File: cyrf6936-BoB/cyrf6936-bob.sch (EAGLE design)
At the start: 23 parts

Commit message: Added revision and author
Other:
- note added: "Joseph Moreland"
- note added: "v0.1"
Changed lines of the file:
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@@
 Load Capacitance 10pF
 </text>
+<text x="182.88" y="7.62" size="2.1844" layer="97">Joseph Moreland</text>
+<text x="236.22" y="7.62" size="2.1844" layer="97">v0.1</text>
 </plain>
 <instances>

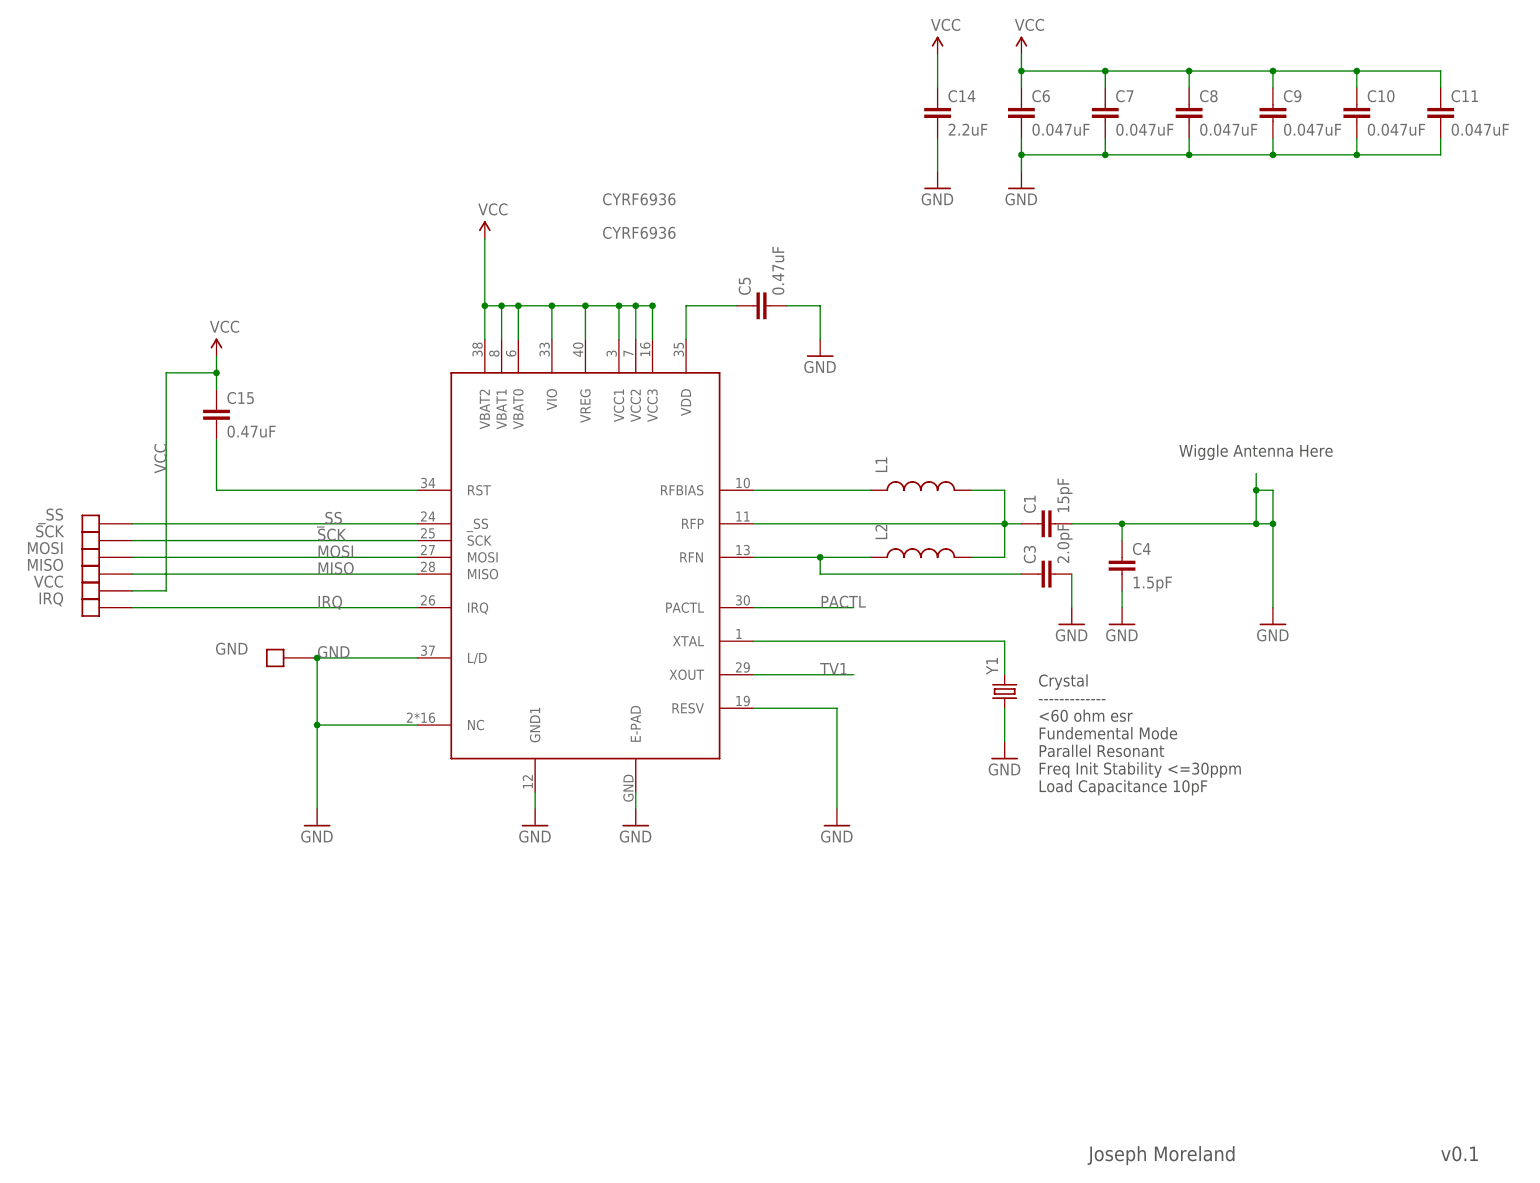
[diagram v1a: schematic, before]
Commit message: Screwed up that last commit.  this update include changes to the production gerber folders.  Adds hackvana to the cyrf6936-BoB and cleans up the fab notes a bit.  Still need to standardize and parameterize the creation of the gerbers.
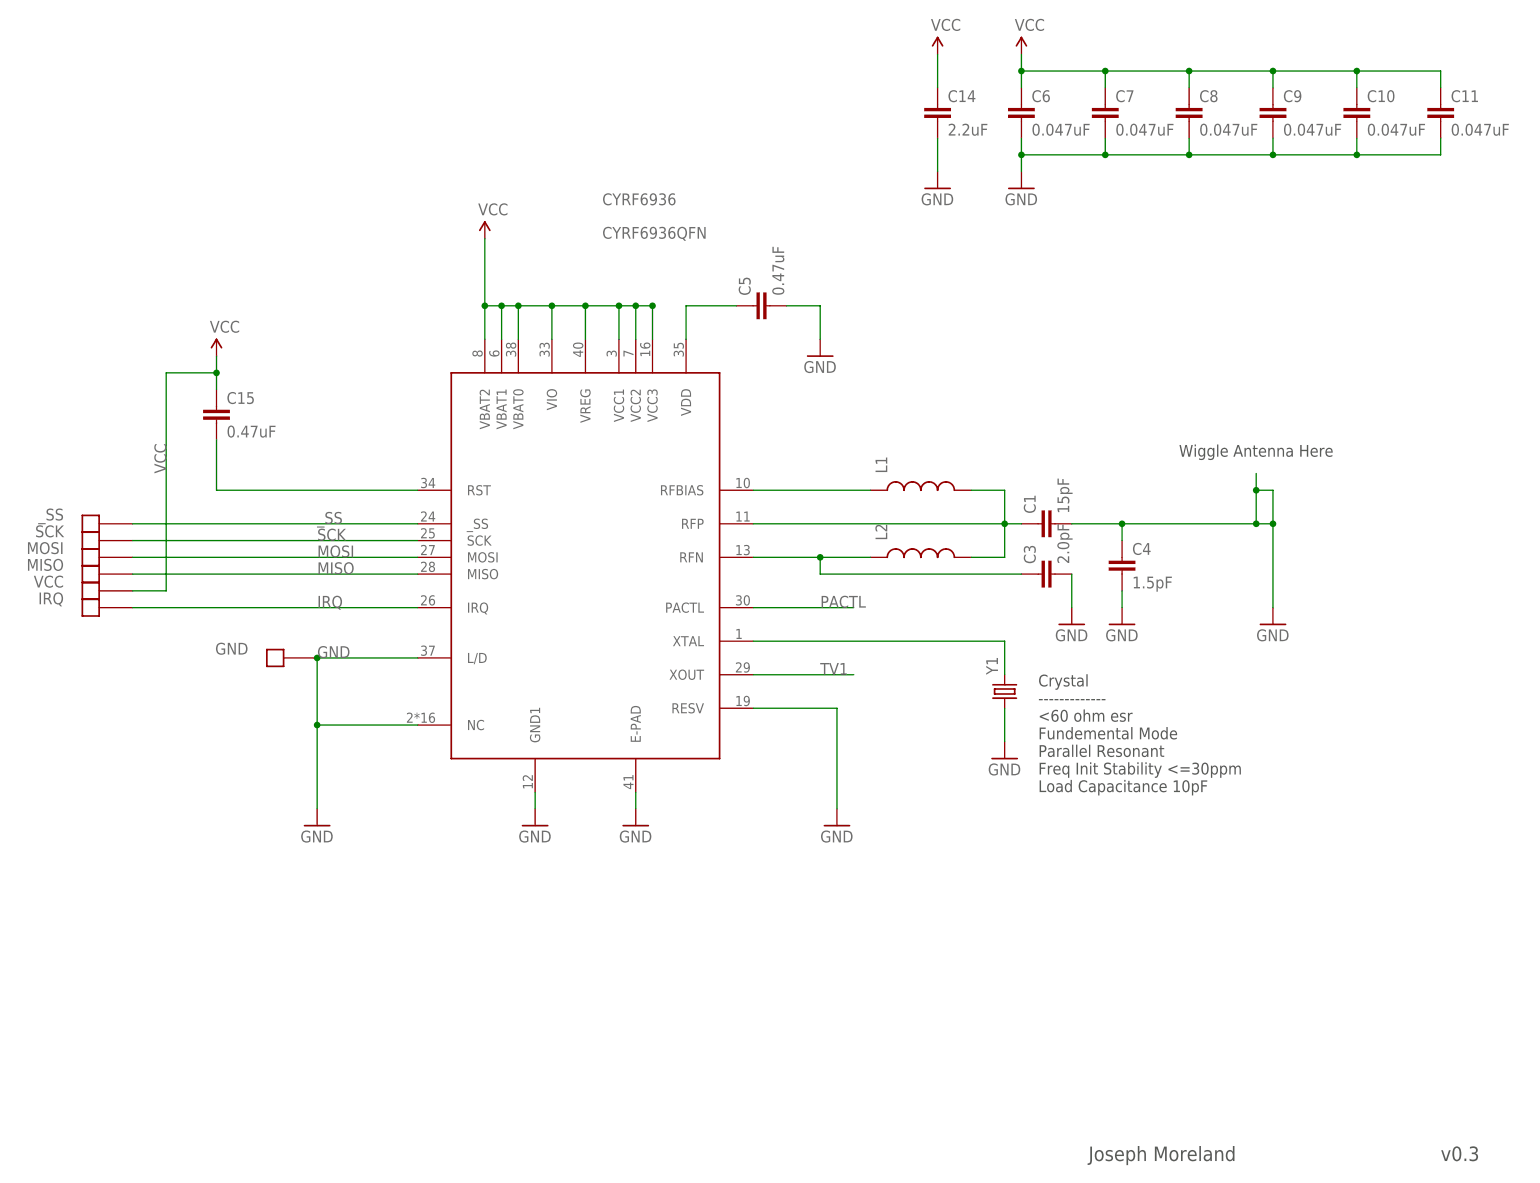
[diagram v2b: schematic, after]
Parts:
- C1, C10, C11, C15, C3, C4, C5, C6, C7, C8, C9: device SparkFun-Passives:CAP0402-CAP -> JCM-Capacitors:CAP0402-CAP
- C14: device SparkFun-Passives:CAP0805 -> JCM-Capacitors:CAP0805
- CYRF6936: value CYRF6936 -> CYRF6936QFN; device JCM:CYRF6936 -> JCM-IC:CYRF6936QFN
- GND, IRQ, MISO, MOSI, SCK, VCC, _SS: value SOLDER_PAD -> SOLDER_PADTH; device JCM:SOLDER_PAD -> JCM-Connectors:SOLDER_PADTH
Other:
- note added: "v0.3"
- note removed: "v0.1"
- moved on the sheet: CYRF6936
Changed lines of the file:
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@@
 </variantdefs>
 <classes>
-<class number="0" name="default" width="0" drill="0">
+<class number="0" name="default" width="0.2032" drill="0.3048">
 </class>
 </classes>
 <parts>
-<part name="CYRF6936" library="JCM" deviceset="CYRF6936" device="">
+<part name="CYRF6936" library="JCM-IC" deviceset="CYRF6936" device="QFN" value="CYRF6936QFN">
 <attribute name="PARTNO" value="CYRF6936B-40LTXC"/>
 </part>
@@
 <part name="GND4" library="SparkFun-Aesthetics" deviceset="GND" device=""/>
 <part name="SUPPLY1" library="SparkFun-Aesthetics" deviceset="VCC" device=""/>
-<part name="C5" library="SparkFun-Passives" deviceset="CAP" device="0402-CAP" value="0.47uF">
+<part name="C5" library="JCM-Capacitors" deviceset="CAP" device="0402-CAP" value="0.47uF">
 <attribute name="PARTNO" value="GRM155R60J474KE19D"/>
 <attribute name="VOLT" value="6.3"/>
 </part>
 <part name="GND5" library="SparkFun-Aesthetics" deviceset="GND" device=""/>
-<part name="C15" library="SparkFun-Passives" deviceset="CAP" device="0402-CAP" value="0.47uF">
+<part name="C15" library="JCM-Capacitors" deviceset="CAP" device="0402-CAP" value="0.47uF">
 <attribute name="PARTNO" value="GRM155R60J474KE19D"/>
 <attribute name="VOLT" value="6.3"/>
@@
 <attribute name="PARTNO" value="ELJ-RF1N8DFB"/>
 </part>
-<part name="C1" library="SparkFun-Passives" deviceset="CAP" device="0402-CAP" value="15pF">
+<part name="C1" library="JCM-Capacitors" deviceset="CAP" device="0402-CAP" value="15pF">
 <attribute name="PARTNO" value="C0402C150J5GACTU"/>
 <attribute name="VOLT" value="50"/>
 </part>
-<part name="C3" library="SparkFun-Passives" deviceset="CAP" device="0402-CAP" value="2.0pF">
+<part name="C3" library="JCM-Capacitors" deviceset="CAP" device="0402-CAP" value="2.0pF">
 <attribute name="PARTNO" value="C0402C209C5GACTU"/>
 <attribute name="VOLT" value="50"/>
 </part>
-<part name="C4" library="SparkFun-Passives" deviceset="CAP" device="0402-CAP" value="1.5pF">
+<part name="C4" library="JCM-Capacitors" deviceset="CAP" device="0402-CAP" value="1.5pF">
 <attribute name="PARTNO" value="C0402C159B5GACTU"/>
 <attribute name="VOLT" value="50"/>
@@
 </part>
 <part name="GND9" library="SparkFun-Aesthetics" deviceset="GND" device=""/>
-<part name="C6" library="SparkFun-Passives" deviceset="CAP" device="0402-CAP" value="0.047uF">
+<part name="C6" library="JCM-Capacitors" deviceset="CAP" device="0402-CAP" value="0.047uF">
 <attribute name="PARTNO" value="0402YD473KAT2A"/>
 </part>
-<part name="C7" library="SparkFun-Passives" deviceset="CAP" device="0402-CAP" value="0.047uF">
+<part name="C7" library="JCM-Capacitors" deviceset="CAP" device="0402-CAP" value="0.047uF">
 <attribute name="PARTNO" value="0402YD473KAT2A"/>
 </part>
-<part name="C8" library="SparkFun-Passives" deviceset="CAP" device="0402-CAP" value="0.047uF">
+<part name="C8" library="JCM-Capacitors" deviceset="CAP" device="0402-CAP" value="0.047uF">
 <attribute name="PARTNO" value="0402YD473KAT2A"/>
 </part>
-<part name="C9" library="SparkFun-Passives" deviceset="CAP" device="0402-CAP" value="0.047uF">
+<part name="C9" library="JCM-Capacitors" deviceset="CAP" device="0402-CAP" value="0.047uF">
 <attribute name="PARTNO" value="0402YD473KAT2A"/>
 </part>
-<part name="C10" library="SparkFun-Passives" deviceset="CAP" device="0402-CAP" value="0.047uF">
+<part name="C10" library="JCM-Capacitors" deviceset="CAP" device="0402-CAP" value="0.047uF">
 <attribute name="PARTNO" value="0402YD473KAT2A"/>
 </part>
-<part name="C11" library="SparkFun-Passives" deviceset="CAP" device="0402-CAP" value="0.047uF">
+<part name="C11" library="JCM-Capacitors" deviceset="CAP" device="0402-CAP" value="0.047uF">
 <attribute name="PARTNO" value="0402YD473KAT2A"/>
 </part>
@@
 <part name="SUPPLY4" library="SparkFun-Aesthetics" deviceset="VCC" device=""/>
 <part name="GND11" library="SparkFun-Aesthetics" deviceset="GND" device=""/>
-<part name="C14" library="SparkFun-Passives" deviceset="CAP" device="0805" value="2.2uF">
+<part name="C14" library="JCM-Capacitors" deviceset="CAP" device="0805" value="2.2uF">
 <attribute name="PARTNO" value="GRM21BR71A225KA01L"/>
 </part>
-<part name="_SS" library="JCM" deviceset="SOLDER_PAD" device=""/>
-<part name="SCK" library="JCM" deviceset="SOLDER_PAD" device=""/>
-<part name="MOSI" library="JCM" deviceset="SOLDER_PAD" device=""/>
-<part name="MISO" library="JCM" deviceset="SOLDER_PAD" device=""/>
-<part name="VCC" library="JCM" deviceset="SOLDER_PAD" device=""/>
-<part name="IRQ" library="JCM" deviceset="SOLDER_PAD" device=""/>
-<part name="GND" library="JCM" deviceset="SOLDER_PAD" device=""/>
+<part name="_SS" library="JCM-Connectors" deviceset="SOLDER_PAD" device="TH"/>
+<part name="SCK" library="JCM-Connectors" deviceset="SOLDER_PAD" device="TH"/>
+<part name="MOSI" library="JCM-Connectors" deviceset="SOLDER_PAD" device="TH"/>
+<part name="MISO" library="JCM-Connectors" deviceset="SOLDER_PAD" device="TH"/>
+<part name="VCC" library="JCM-Connectors" deviceset="SOLDER_PAD" device="TH"/>
+<part name="IRQ" library="JCM-Connectors" deviceset="SOLDER_PAD" device="TH"/>
+<part name="GND" library="JCM-Connectors" deviceset="SOLDER_PAD" device="TH"/>
 </parts>
 <sheets>
@@
 </text>
 <text x="182.88" y="7.62" size="2.1844" layer="97">Joseph Moreland</text>
-<text x="236.22" y="7.62" size="2.1844" layer="97">v0.1</text>
+<text x="236.22" y="7.62" size="2.1844" layer="97">v0.3</text>
 </plain>
 <instances>
